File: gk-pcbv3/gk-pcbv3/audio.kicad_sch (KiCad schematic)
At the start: 33 parts, among them J5 AudioJack3_SwitchTR, J6 Conn_01x02, U12 PAM8302AAS, U14 TPA6110A2DGN, U7 PCM1753DBQ

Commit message: v3 board
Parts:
- removed C88, C89: 10u, Capacitor_SMD:C_0805_2012Metric, symbol Device:C
- removed FB1: FerriteBead, Resistor_SMD:R_0603_1608Metric, symbol Device:FerriteBead
- added C12, C8: 100n, Capacitor_SMD:C_0603_1608Metric, symbol Device:C
- added TP14: TestPoint, TestPoint:TestPoint_Pad_D1.0mm, symbol Connector:TestPoint
- added U19: CDCE913PWR, PW14, symbol CDCE913:CDCE913PWR
- added Y3: 27M, Crystal:Crystal_SMD_SeikoEpson_TSX3225-4Pin_3.2x2.5mm, symbol Device:Crystal_GND24
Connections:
- net GND: now also C12.2, C8.2, U19.10 (GND), U19.5 (GND), Y3.2, Y3.4
- net VCC: now also C8.1, U19.6 (VDDOUT), U19.7 (VDDOUT)
- net PCM_NSS renamed SPI2_NSS
- new net: U19.1 (XIN/CLK), Y3.1
- new net: U19.14 (XOUT), Y3.3
- new net +1V8: C12.1, U19.2 (S0), U19.3 (VDD)
- new net I2C2_SCL: U19.12 (S2/SCL)
- new net I2C2_SDA: U19.13 (S1/SDA)
- new net I2S_CKIN: TP14.1, U19.11 (Y1)
- no-connect marks 1 -> 4
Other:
- note removed: "Analogue filtered VCC Similarly, analogue ground is on same net as GND, but on PCB make it shielded polygon"
- moved on the sheet: R71

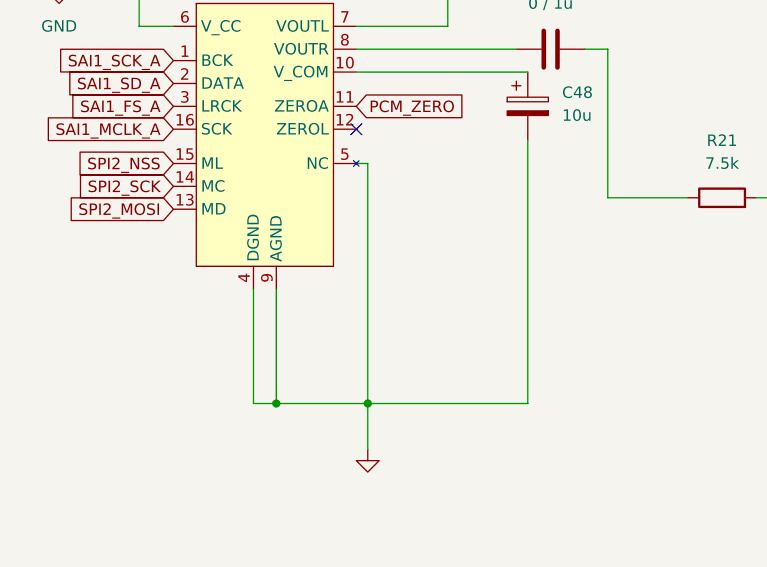
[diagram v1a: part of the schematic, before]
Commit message: redesign for better signal integrity
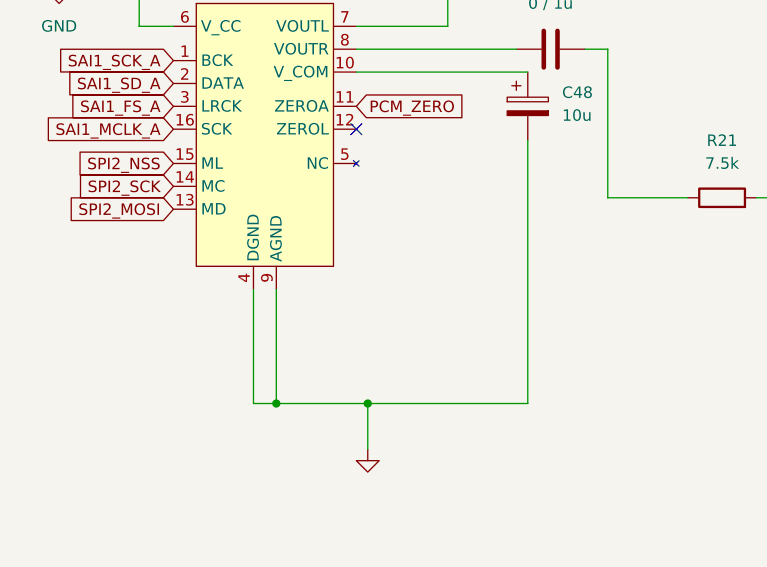
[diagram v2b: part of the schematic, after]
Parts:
- U19: footprint PW14 -> STM32H7S7:PW14
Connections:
- net GND: no longer U7.5 (NC)
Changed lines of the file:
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@@
 	(wire
 		(pts
-			(xy 59.69 68.58) (xy 59.69 95.25)
-		)
-		(stroke
-			(width 0)
-			(type default)
-		)
-	)
-	(wire
-		(pts
 			(xy 220.98 82.55) (xy 220.98 88.9)
 		)
@@
 	(wire
 		(pts
-			(xy 58.42 68.58) (xy 59.69 68.58)
-		)
-		(stroke
-			(width 0)
-			(type default)
-		)
-	)
-	(wire
-		(pts
 			(xy 146.05 85.09) (xy 152.4 85.09)
 		)
@@
 			)
 		)
-		(property "Footprint" "PW14"
+		(property "Footprint" "STM32H7S7:PW14"
 			(at 196.85 105.41 0)
 			(effects

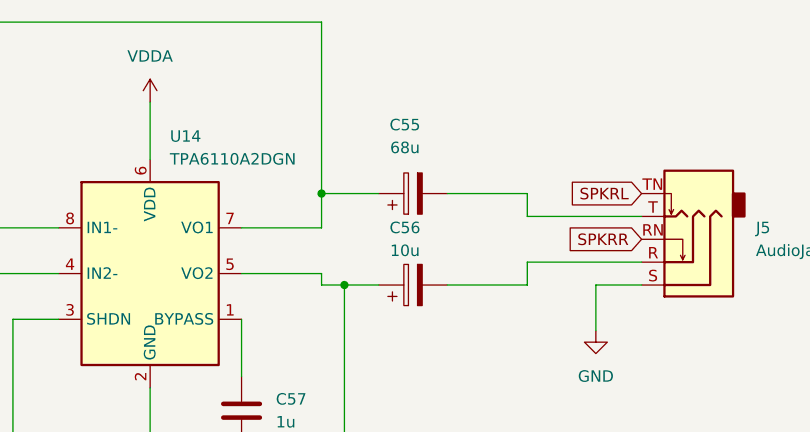
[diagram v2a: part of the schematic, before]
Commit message: update schematics for new vreg design
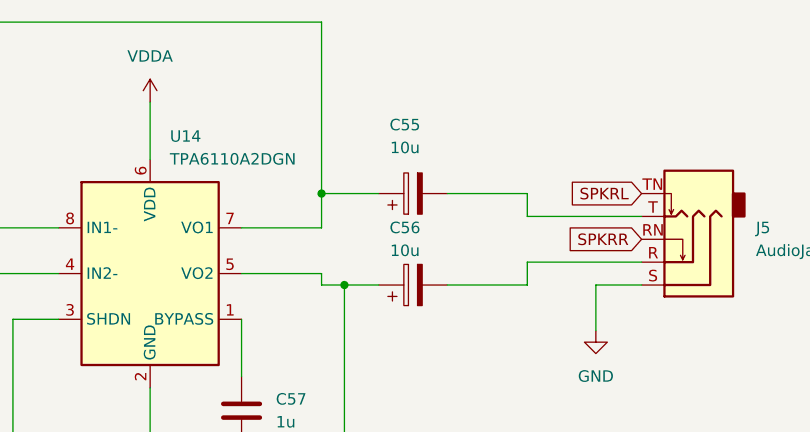
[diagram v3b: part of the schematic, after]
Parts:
- C55: value 68u -> 10u
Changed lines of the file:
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@@
 			)
 		)
-		(property "Value" "68u"
+		(property "Value" "10u"
 			(at 183.261 33.02 90)
 			(effects
